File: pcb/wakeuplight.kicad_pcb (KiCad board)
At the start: 2 copper layers, 113.1 x 44.7 mm, 81 parts, among them J1 691322310002, J11 PCM5102A Breakout, J12 Conn_01x03_Pin, J13 USB_A, J2 Conn_01x19, J3 Conn_01x19, J4 MPT 2,54, J5 MPT 2,54, J6 MKDS 3.5mm, J7 MKDS 3.5mm, J8 MKDS 3.5mm, J9 MKDS 3.5mm, Q1 T2N7002BK, Q2 PSMN1R2-30YLC, Q3 PSMN1R2-30YLC, U1 MCP14A0302, U2 MCP14A0302, U3 LMR16006YQ, U4 LMR16006YQ

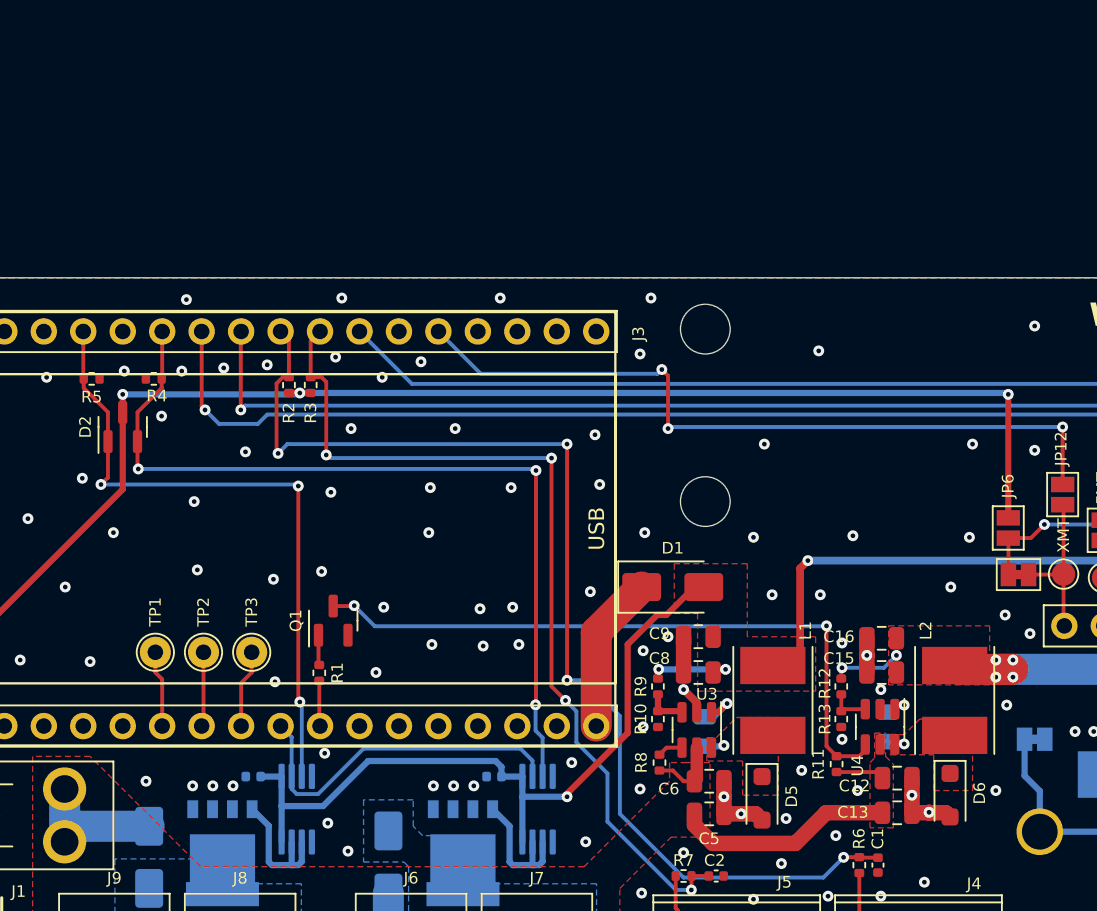
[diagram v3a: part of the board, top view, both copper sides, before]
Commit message: moved to Kicad 8
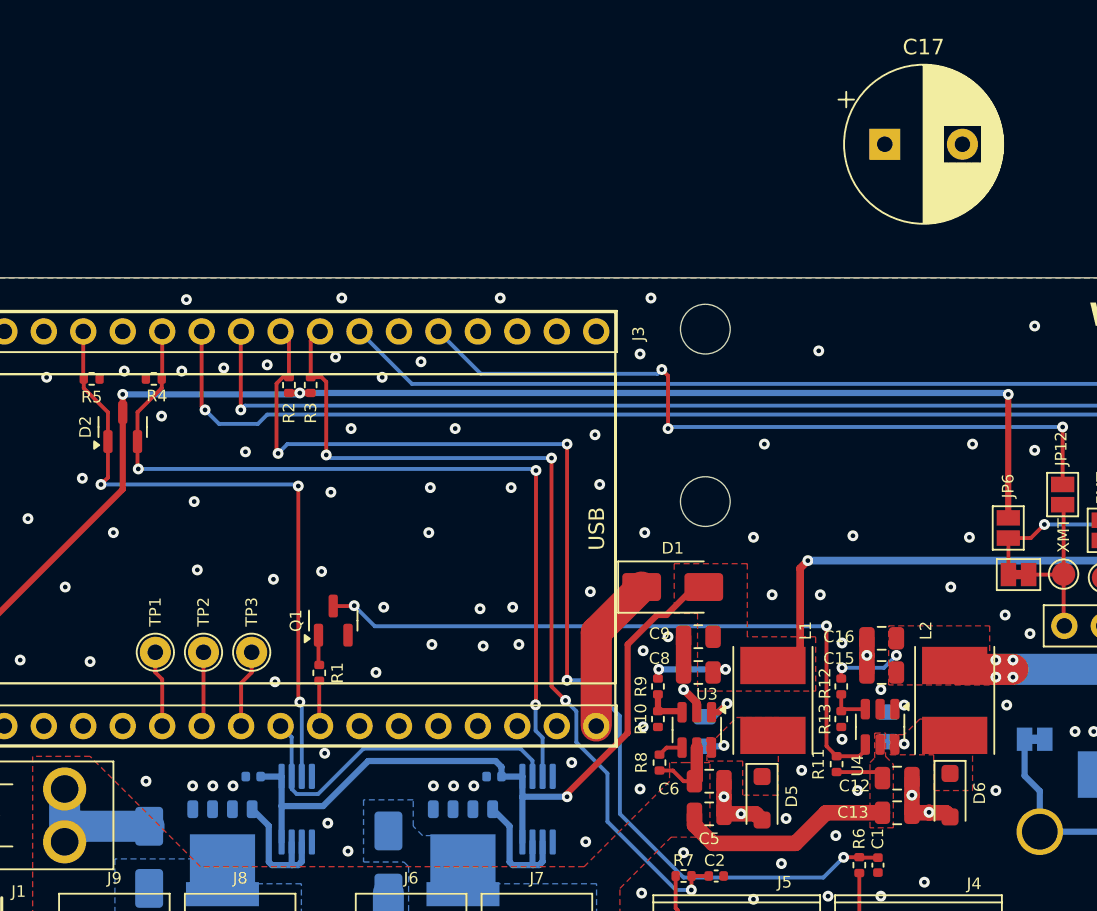
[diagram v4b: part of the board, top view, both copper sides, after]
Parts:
- added C17: ? uF, Capacitor_THT:CP_Radial_D10.0mm_P5.00mm, F.Cu at (72.5, -8.60)
